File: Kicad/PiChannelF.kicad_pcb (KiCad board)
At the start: 2 copper layers, 77 x 117.8 mm, 8 parts, among them J1 Conn_01x20, J2 Conn_01x20, SW1 SW_Push

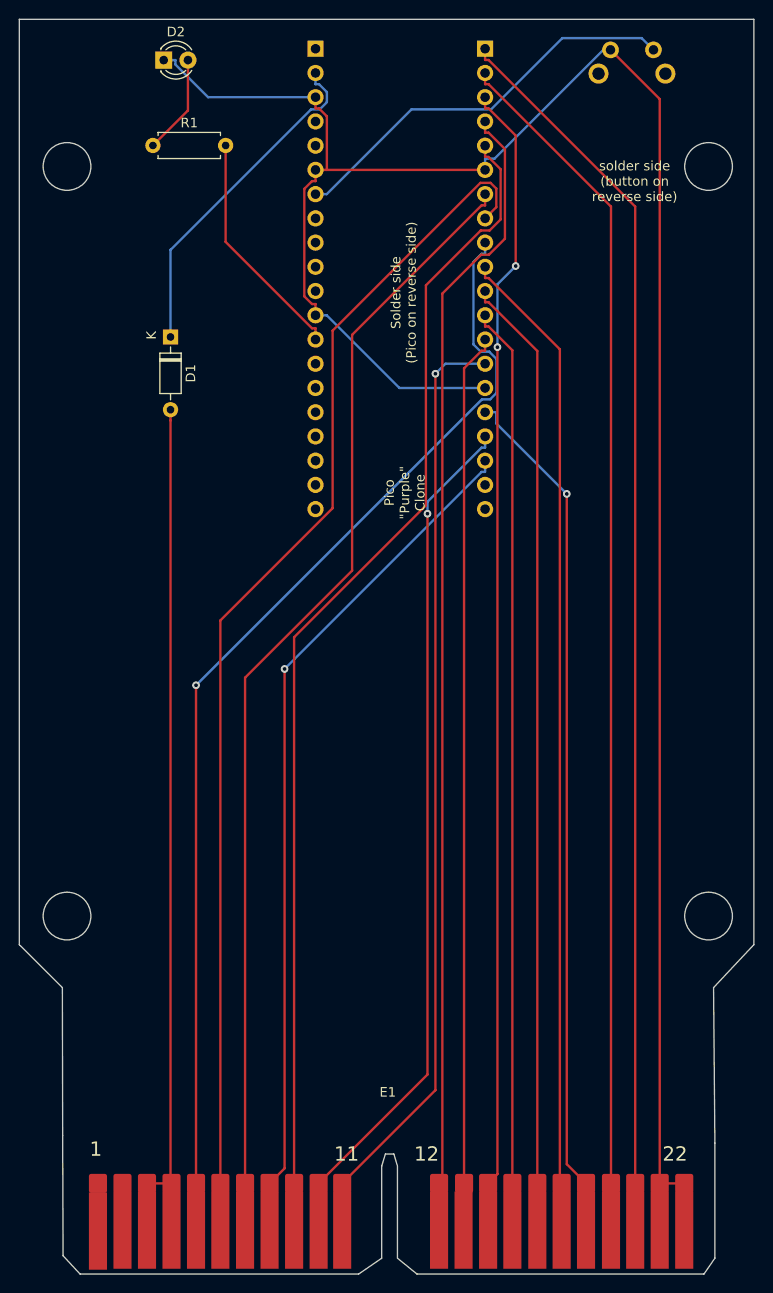
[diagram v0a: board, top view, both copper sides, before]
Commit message: Add files via upload
little shift and enlarge of holes for screw in pcb
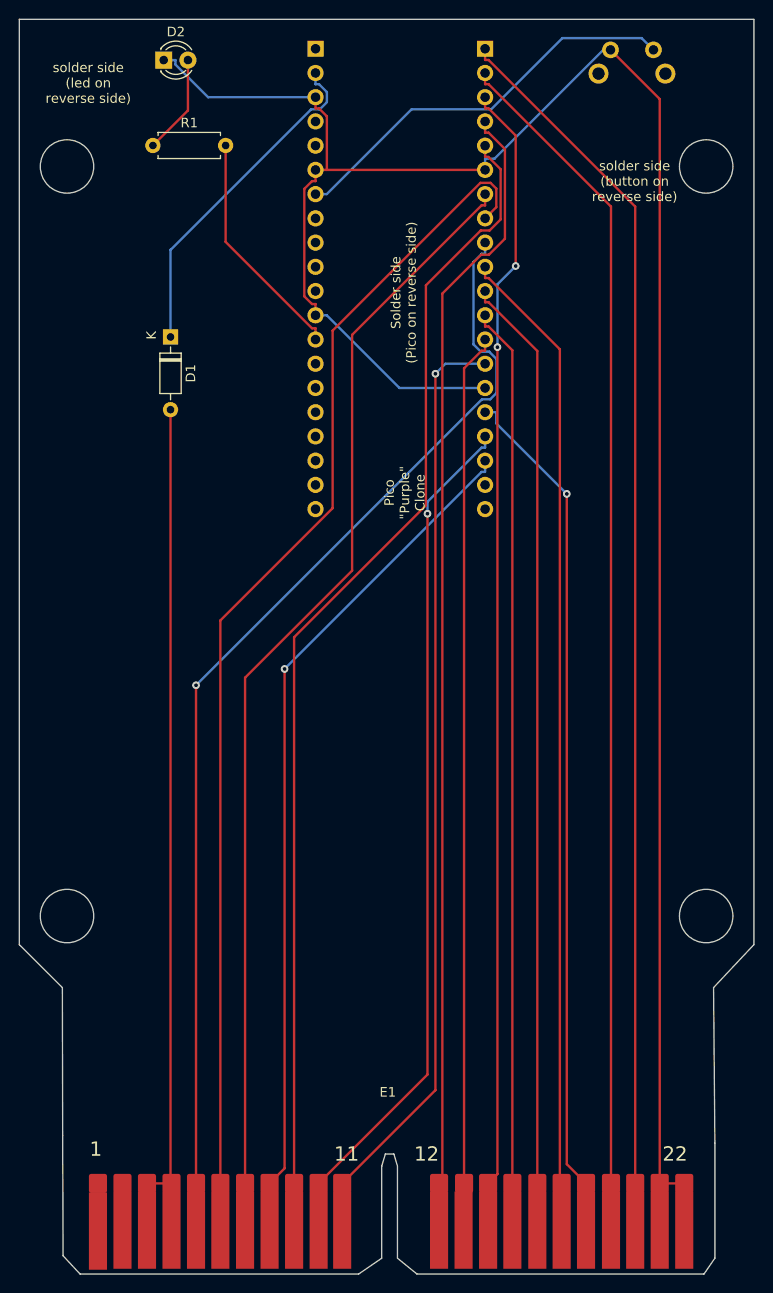
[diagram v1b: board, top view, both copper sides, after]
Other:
- outline, holes or cut-outs redrawn
- board text added: "solder side (led on reverse side)"
